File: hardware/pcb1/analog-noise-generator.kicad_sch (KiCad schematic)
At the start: 91 parts, among them J1 USB_C_Receptacle_USB2.0, J2 Conn_01x03_Pin, J3 PJ-211A, J4 PJ-211A, J5 Conn_01x04_Pin, J6 Conn_01x04_Pin, J7 Conn_01x02_Pin, J9 Conn_02x04_Odd_Even, U1 STM32F072CBTx, U2 USBLC6-2SC6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

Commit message: finish routing
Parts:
- added TP10: AGND, analog-noise-generator:TestPoint_THTPad_small, symbol Connector:TestPoint_Probe
- added TP11: AVCC, analog-noise-generator:TestPoint_THTPad_small, symbol Connector:TestPoint_Probe
- added TP9: GND, analog-noise-generator:TestPoint_THTPad_small, symbol Connector:TestPoint_Probe
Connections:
- net AGND: now also TP10.1
- net AVCC: now also TP11.1
- net EPD_CS: now also U1.4 (PC15); no longer U1.5 (PF0)
- net EPD_DC: now also U1.6 (PF1); no longer U1.4 (PC15)
- net EPD_RES: now also U1.5 (PF0); no longer U1.6 (PF1)
- net GND: now also TP9.1
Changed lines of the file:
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@@
   (junction (at 123.19 20.32) (diameter 0) (color 0 0 0 0)
   )
+  (junction (at 265.43 26.67) (diameter 0) (color 0 0 0 0)
+  )
   (junction (at 55.88 22.86) (diameter 0) (color 0 0 0 0)
   )
@@
   (junction (at 64.77 22.86) (diameter 0) (color 0 0 0 0)
   )
+  (junction (at 55.88 33.02) (diameter 0) (color 0 0 0 0)
+  )
   (junction (at 60.96 86.36) (diameter 0) (color 0 0 0 0)
   )
@@
   (junction (at 251.46 41.91) (diameter 0) (color 0 0 0 0)
   )
+  (junction (at 264.16 41.91) (diameter 0) (color 0 0 0 0)
+  )
   (junction (at 55.88 54.61) (diameter 0) (color 0 0 0 0)
   )
@@
     (stroke (width 0) (type default))
   )
-  (wire (pts (xy 261.62 26.67) (xy 273.05 26.67))
+  (wire (pts (xy 261.62 26.67) (xy 265.43 26.67))
     (stroke (width 0) (type default))
   )
@@
     (stroke (width 0) (type default))
   )
-  (wire (pts (xy 261.62 41.91) (xy 273.05 41.91))
+  (wire (pts (xy 261.62 41.91) (xy 264.16 41.91))
     (stroke (width 0) (type default))
   )
@@
     (stroke (width 0) (type default))
   )
+  (wire (pts (xy 265.43 26.67) (xy 273.05 26.67))
+    (stroke (width 0) (type default))
+  )
   (wire (pts (xy 104.14 20.32) (xy 105.41 20.32))
     (stroke (width 0) (type default))
@@
     (stroke (width 0) (type default))
   )
+  (wire (pts (xy 264.16 41.91) (xy 273.05 41.91))
+    (stroke (width 0) (type default))
+  )
   (wire (pts (xy 120.65 80.01) (xy 125.73 80.01))
     (stroke (width 0) (type default))
@@
     (effects (font (size 1.27 1.27)) (justify left bottom))
   )
-  (label "EPD_DC" (at 115.57 74.93 0) (fields_autoplaced)
+  (label "EPD_DC" (at 115.57 64.77 0) (fields_autoplaced)
     (effects (font (size 1.27 1.27)) (justify left bottom))
   )
@@
     (effects (font (size 1.27 1.27)) (justify left bottom))
   )
-  (label "EPD_RES" (at 115.57 64.77 0) (fields_autoplaced)
+  (label "EPD_RES" (at 115.57 62.23 0) (fields_autoplaced)
     (effects (font (size 1.27 1.27)) (justify left bottom))
   )
@@
     (effects (font (size 1.27 1.27)) (justify right bottom))
   )
-  (label "EPD_CS" (at 115.57 62.23 0) (fields_autoplaced)
+  (label "EPD_CS" (at 115.57 74.93 0) (fields_autoplaced)
     (effects (font (size 1.27 1.27)) (justify left bottom))
   )
@@
     )
   )
+  (symbol (lib_id "Connector:TestPoint_Probe") (at 265.43 26.67 0) (unit 1)
+    (in_bom no) (on_board yes) (dnp no)
+    (property "Reference" "TP11" (at 269.24 22.86 0)
+      (effects (font (size 1.27 1.27)) (justify left))
+    )
+    (property "Value" "AVCC" (at 269.24 25.4 0)
+      (effects (font (size 1.27 1.27)) (justify left))
+    )
+    (property "Footprint" "analog-noise-generator:TestPoint_THTPad_small" (at 270.51 26.67 0)
+      (effects (font (size 1.27 1.27)) hide)
+    )
+    (property "Datasheet" "~" (at 270.51 26.67 0)
+      (effects (font (size 1.27 1.27)) hide)
+    )
+    (pin "1")
+    (instances
+      (project "analog-noise-generator"
+        (path "/e71fa5ad-0f80-45ec-aa84-70ffc489027a"
+          (reference "TP11") (unit 1)
+        )
+      )
+    )
+  )
   (symbol (lib_id "power:VBUS") (at 60.96 76.2 0) (unit 1)
     (in_bom yes) (on_board yes) (dnp no) (fields_autoplaced)
@@
     )
   )
+  (symbol (lib_id "Connector:TestPoint_Probe") (at 55.88 33.02 0) (mirror x) (unit 1)
+    (in_bom no) (on_board yes) (dnp no)
+    (property "Reference" "TP9" (at 59.69 36.83 0)
+      (effects (font (size 1.27 1.27)) (justify left))
+    )
+    (property "Value" "GND" (at 59.69 34.29 0)
+      (effects (font (size 1.27 1.27)) (justify left))
+    )
+    (property "Footprint" "analog-noise-generator:TestPoint_THTPad_small" (at 60.96 33.02 0)
+      (effects (font (size 1.27 1.27)) hide)
+    )
+    (property "Datasheet" "~" (at 60.96 33.02 0)
+      (effects (font (size 1.27 1.27)) hide)
+    )
+    (pin "1")
+    (instances
+      (project "analog-noise-generator"
+        (path "/e71fa5ad-0f80-45ec-aa84-70ffc489027a"
+          (reference "TP9") (unit 1)
+        )
+      )
+    )
+  )
   (symbol (lib_id "power:GND") (at 40.64 154.94 0) (unit 1)
     (in_bom yes) (on_board yes) (dnp no) (fields_autoplaced)
@@
         )
       )
+    )
+  )
+  (symbol (lib_id "Connector:TestPoint_Probe") (at 264.16 41.91 0) (mirror x) (unit 1)
+    (in_bom no) (on_board yes) (dnp no)
+    (property "Reference" "TP10" (at 267.97 45.72 0)
+      (effects (font (size 1.27 1.27)) (justify left))
+    )
+    (property "Value" "AGND" (at 267.97 43.18 0)
+      (effects (font (size 1.27 1.27)) (justify left))
+    )
+    (property "Footprint" "analog-noise-generator:TestPoint_THTPad_small" (at 269.24 41.91 0)
+      (effects (font (size 1.27 1.27)) hide)
+    )
+    (property "Datasheet" "~" (at 269.24 41.91 0)
+      (effects (font (size 1.27 1.27)) hide)
+    )
+    (pin "1")
+    (instances
+      (project "analog-noise-generator"
+        (path "/e71fa5ad-0f80-45ec-aa84-70ffc489027a"
+          (reference "TP10") (unit 1)
+        )
+      )

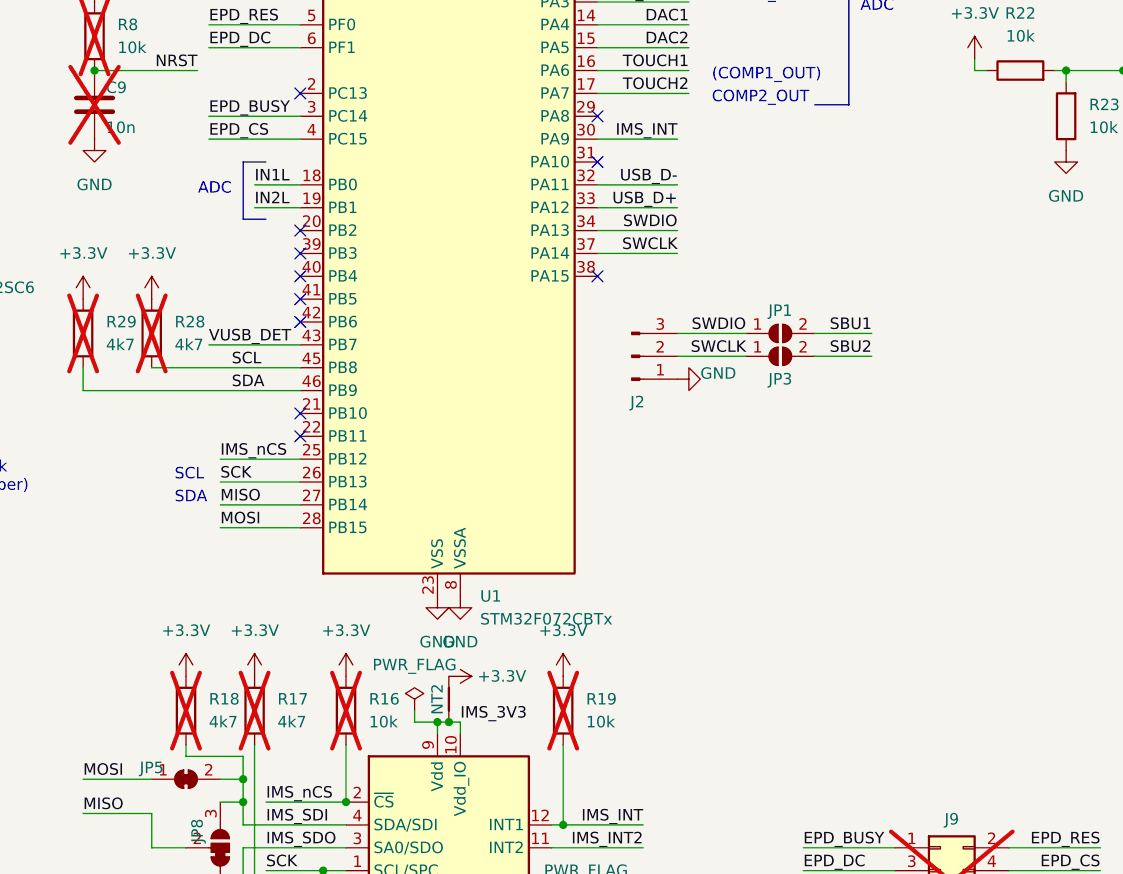
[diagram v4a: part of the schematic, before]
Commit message: add some LEDs
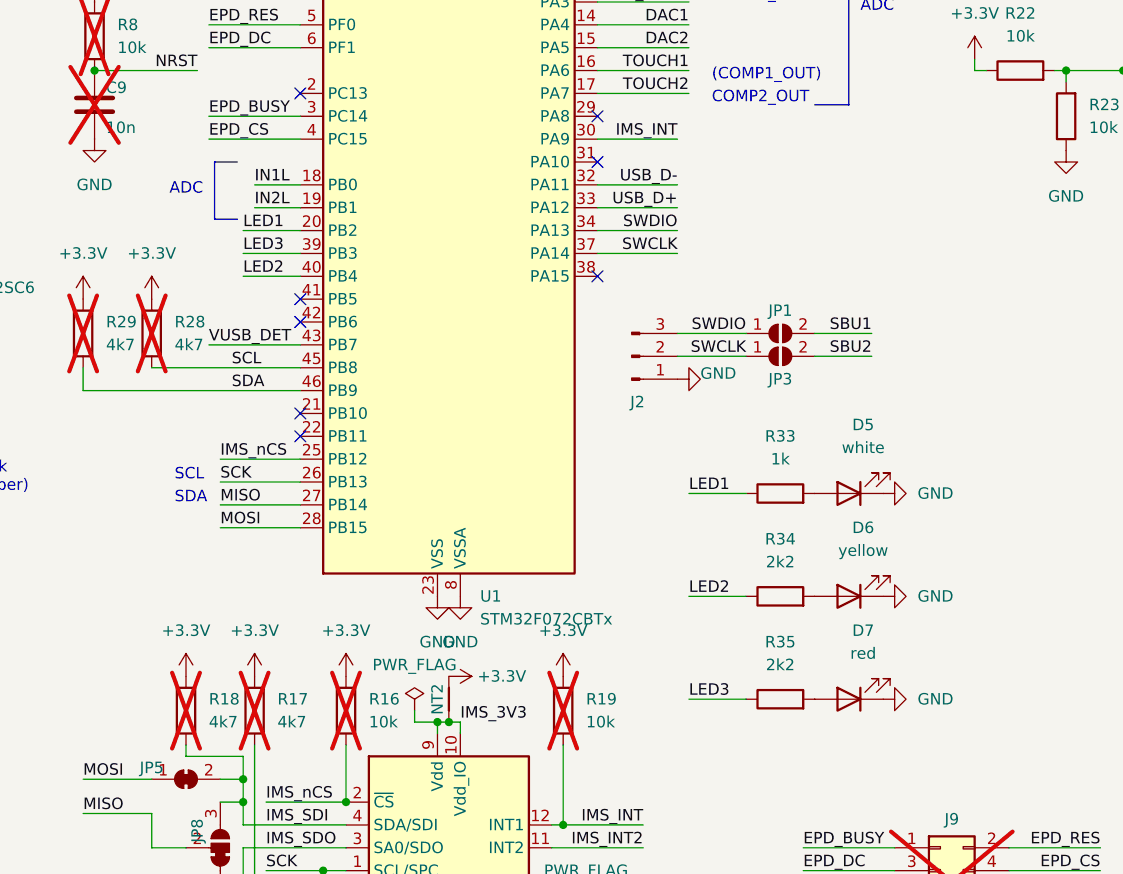
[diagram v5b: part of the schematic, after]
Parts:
- added D5: white, LED_SMD:LED_0603_1608Metric, symbol Device:LED
- added D6: yellow, LED_SMD:LED_0603_1608Metric, symbol Device:LED
- added D7: red, LED_SMD:LED_0603_1608Metric, symbol Device:LED
- added R33: 1k, Resistor_SMD:R_0402_1005Metric, symbol Device:R
- added R34, R35: 2k2, Resistor_SMD:R_0402_1005Metric, symbol Device:R
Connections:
- net GND: now also D5.1 (K), D6.1 (K), D7.1 (K)
- net LED1: now reaches U1.20 (PB2)
- net LED1: now also R33.1
- net LED3: now reaches U1.39 (PB3)
- net LED3: now also R35.1
- net LED2: now reaches U1.40 (PB4)
- net LED2: now also R34.1
- new net: D7.2 (A), R35.2
- new net: D5.2 (A), R33.2
- new net: D6.2 (A), R34.2
- no-connect marks 16 -> 13

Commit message: add testpoint for 3.3V
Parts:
- added TP12: 3V3, TestPoint:TestPoint_Pad_1.0x1.0mm, symbol Connector:TestPoint_Probe
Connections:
- net +3.3V: now also TP12.1
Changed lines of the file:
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@@
+    )
+  )
+  (symbol (lib_id "Connector:TestPoint_Probe") (at 242.57 127 0) (unit 1)
+    (in_bom no) (on_board yes) (dnp no)
+    (property "Reference" "TP12" (at 246.38 123.19 0)
+      (effects (font (size 1.27 1.27)) (justify left))
+    )
+    (property "Value" "3V3" (at 246.38 125.73 0)
+      (effects (font (size 1.27 1.27)) (justify left))
+    )
+    (property "Footprint" "TestPoint:TestPoint_Pad_1.0x1.0mm" (at 247.65 127 0)
+      (effects (font (size 1.27 1.27)) hide)
+    )
+    (property "Datasheet" "~" (at 247.65 127 0)
+      (effects (font (size 1.27 1.27)) hide)
+    )
+    (pin "1")
+    (instances
+      (project "analog-noise-generator"
+        (path "/e71fa5ad-0f80-45ec-aa84-70ffc489027a"
+          (reference "TP12") (unit 1)
+        )
+      )
     )
   )
@@
         )
       )
+    )
+  )
+  (symbol (lib_id "power:+3.3V") (at 242.57 127 90) (unit 1)
+    (in_bom yes) (on_board yes) (dnp no) (fields_autoplaced)
+    (property "Reference" "#PWR077" (at 246.38 127 0)
+      (effects (font (size 1.27 1.27)) hide)
+    )
+    (property "Value" "+3.3V" (at 239.395 127 90)
+      (effects (font (size 1.27 1.27)) (justify left))
+    )
+    (property "Footprint" "" (at 242.57 127 0)
+      (effects (font (size 1.27 1.27)) hide)
+    )
+    (property "Datasheet" "" (at 242.57 127 0)
+      (effects (font (size 1.27 1.27)) hide)
+    )
+    (pin "1")
+    (instances
+      (project "analog-noise-generator"
+        (path "/e71fa5ad-0f80-45ec-aa84-70ffc489027a"
+          (reference "#PWR077") (unit 1)
+        )
+      )

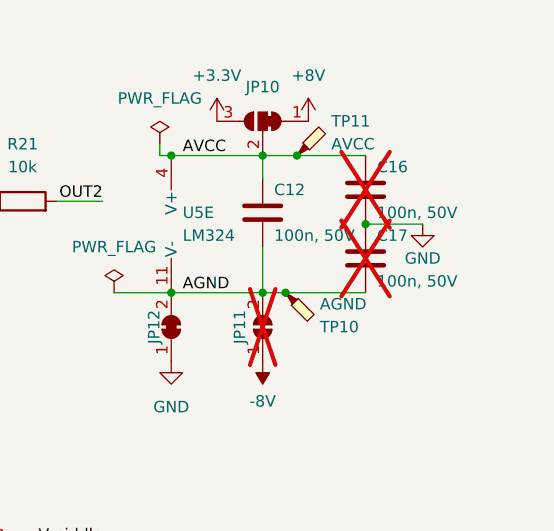
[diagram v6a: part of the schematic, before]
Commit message: fix some issues for JLC
- increase some clearances that were marked as "danger" in their DFM
- change value of C12, so it won't be grouped with the incompatible 100 nF caps
- add image to README
- rotate U2 in CPL file
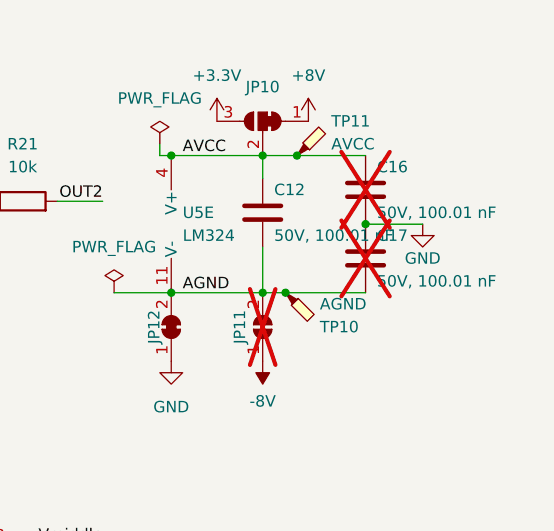
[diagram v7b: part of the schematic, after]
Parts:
- C12, C16, C17: value 100n, 50V -> 50V, 100.01 nF
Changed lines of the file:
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@@
       (effects (font (size 1.27 1.27)) (justify left))
     )
-    (property "Value" "100n, 50V" (at 262.89 35.56 0)
+    (property "Value" "50V, 100.01 nF" (at 262.89 35.56 0)
       (effects (font (size 1.27 1.27)) (justify left))
     )
@@
       (effects (font (size 1.27 1.27)) (justify left))
     )
-    (property "Value" "100n, 50V" (at 274.32 40.64 0)
+    (property "Value" "50V, 100.01 nF" (at 274.32 40.64 0)
       (effects (font (size 1.27 1.27)) (justify left))
     )
@@
       (effects (font (size 1.27 1.27)) (justify left))
     )
-    (property "Value" "100n, 50V" (at 274.32 33.02 0)
+    (property "Value" "50V, 100.01 nF" (at 274.32 33.02 0)
       (effects (font (size 1.27 1.27)) (justify left))
     )
